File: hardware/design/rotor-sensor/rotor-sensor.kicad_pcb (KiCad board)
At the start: 2 copper layers, 42 x 34.7 mm, 92 parts, among them J2 Conn_01x06, J4 Conn_ARM_JTAG_SWD_10, U1 MCP2021A-xxxE/SN, U2 AP22804AW5, U3 BMI088, U4 AP2127K-ADJTRG1, U5 AP22804AW5, U6 ATSAMD21E18A-A, Y1 ABS07-32.768KHZ-7-T

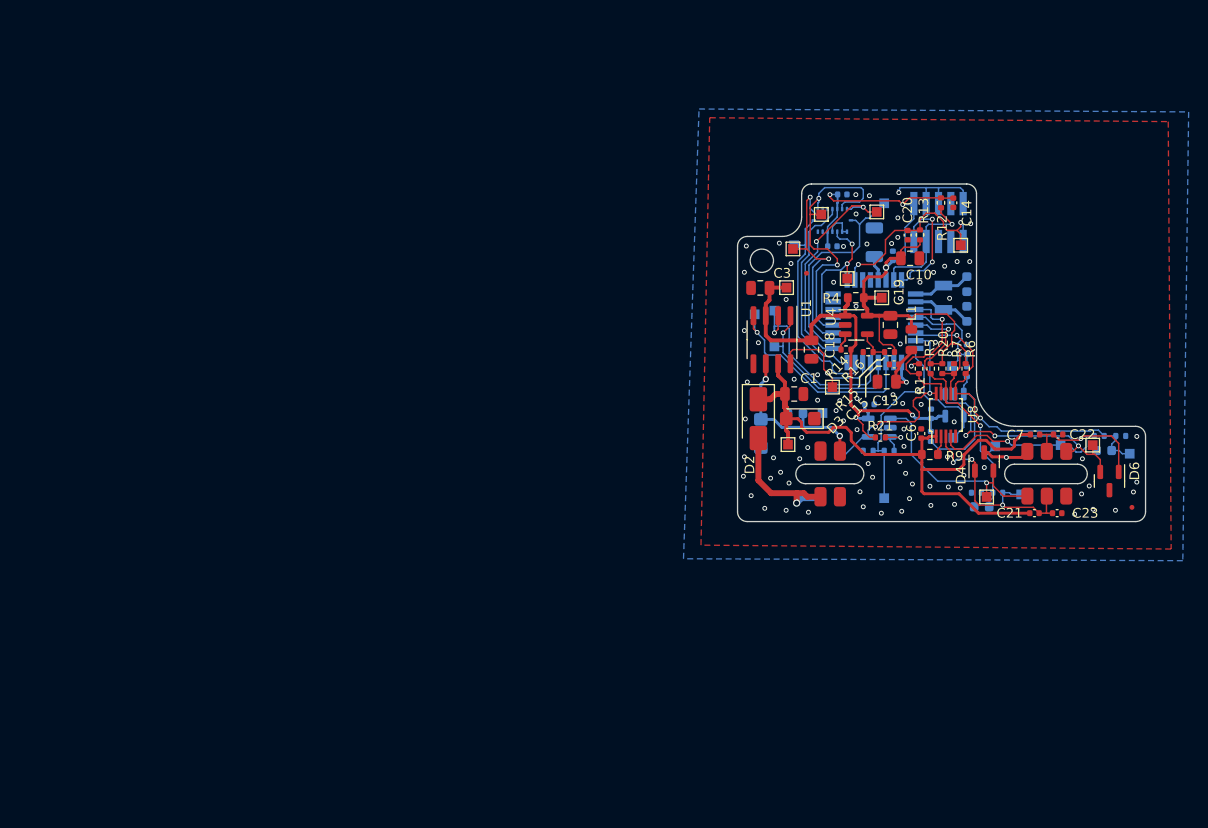
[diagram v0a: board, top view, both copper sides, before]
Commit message: New schematic done
Works with TLIN1028-Q1 transceiver
Added BMP581 pressure sensor
Removed 3wire output stage
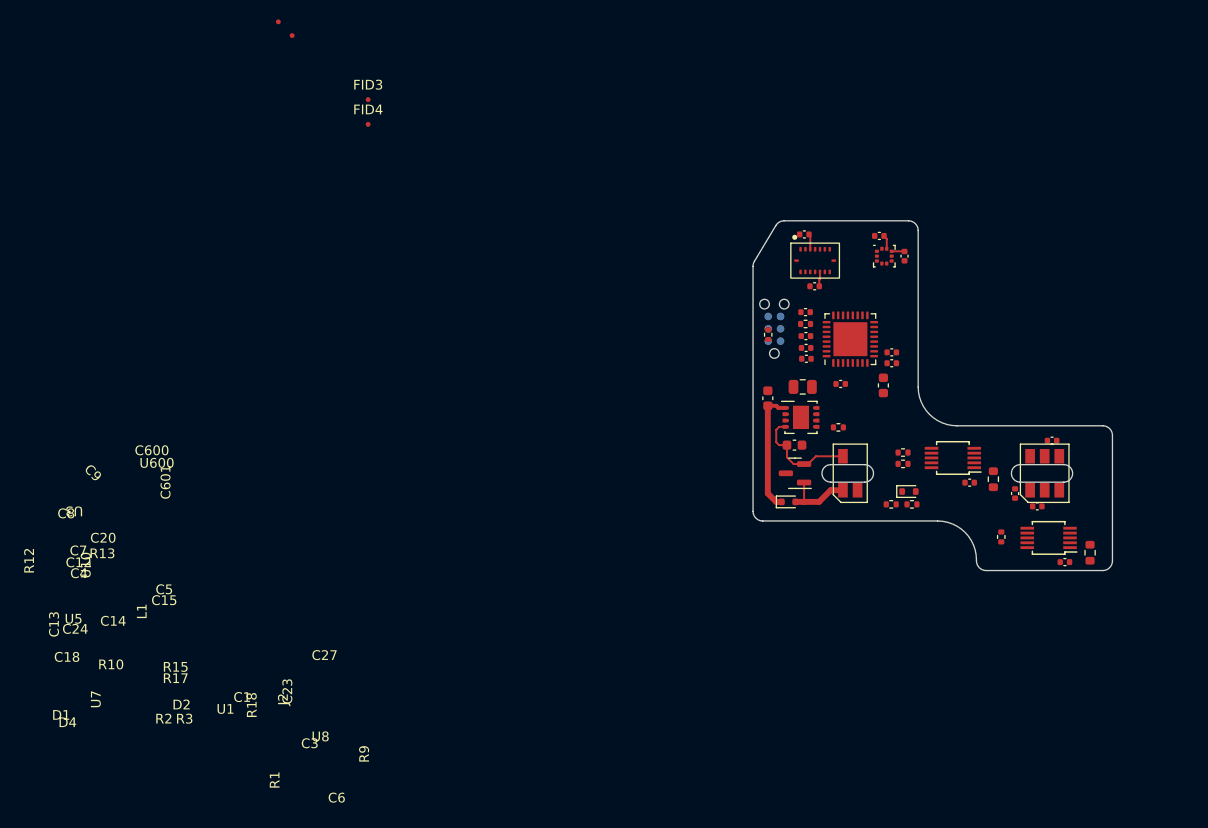
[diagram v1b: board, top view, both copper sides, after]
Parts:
- removed C10, C19: 10u, Capacitor_SMD:C_0805_2012Metric
- removed C11, C16: 6.8p, Capacitor_SMD:C_0603_1608Metric
- removed C17: 1u, Capacitor_SMD:C_1206_3216Metric
- removed C2: 220p, Capacitor_SMD:C_0603_1608Metric
- removed C21, C22: 220n, Capacitor_SMD:C_0402_1005Metric
- removed C25: 22n, Capacitor_SMD:C_0603_1608Metric
- removed D3: SMF33CA-DIO, Diode_SMD:D_SMF
- removed D6: PESD5V0S2BT, Package_TO_SOT_SMD:SOT-23
- removed J4: Conn_ARM_JTAG_SWD_10, Connector_PinHeader_1.27mm:PinHeader_2x05_P1.27mm_Vertical_SMD
- removed R11, R19, R8: 1k, Resistor_SMD:R_0402_1005Metric
- removed R14, R20, R21, R22, R5, R6: 10k, Resistor_SMD:R_0402_1005Metric
- removed R16: 1.5k, Resistor_SMD:R_0402_1005Metric
- removed R4: 0, Resistor_SMD:R_0603_1608Metric
- removed R7: 4.7k, Resistor_SMD:R_0402_1005Metric
- removed TP1: O5, TestPoint:TestPoint_Pad_1.0x1.0mm
- removed TP10: V2, TestPoint:TestPoint_Pad_1.0x1.0mm
- removed TP11: V1, TestPoint:TestPoint_Pad_1.0x1.0mm
- removed TP12: B1, TestPoint:TestPoint_Pad_1.0x1.0mm
- removed TP13: B2, TestPoint:TestPoint_Pad_1.0x1.0mm
- removed TP14: B3, TestPoint:TestPoint_Pad_1.0x1.0mm
- removed TP15: B4, TestPoint:TestPoint_Pad_1.0x1.0mm
- removed TP16: B5, TestPoint:TestPoint_Pad_1.0x1.0mm
- removed TP17: S1, TestPoint:TestPoint_Pad_1.0x1.0mm
- removed TP19: S3, TestPoint:TestPoint_Pad_1.0x1.0mm
- removed TP2: O6, TestPoint:TestPoint_Pad_1.0x1.0mm
- removed TP20: S4, TestPoint:TestPoint_Pad_1.0x1.0mm
- removed TP21: S5, TestPoint:TestPoint_Pad_1.0x1.0mm
- removed TP22: S6, TestPoint:TestPoint_Pad_1.0x1.0mm
- removed TP23: S7, TestPoint:TestPoint_Pad_1.0x1.0mm
- removed TP27: M1, TestPoint:TestPoint_Pad_1.0x1.0mm
- removed TP28: O4, TestPoint:TestPoint_Pad_1.0x1.0mm
- removed TP29: O2, TestPoint:TestPoint_Pad_1.0x1.0mm
- removed TP3: O7, TestPoint:TestPoint_Pad_1.0x1.0mm
- removed TP30: O1, TestPoint:TestPoint_Pad_1.0x1.0mm
- removed TP4: O8, TestPoint:TestPoint_Pad_1.0x1.0mm
- removed TP5: O9, TestPoint:TestPoint_Pad_1.0x1.0mm
- removed TP6: O10, TestPoint:TestPoint_Pad_1.0x1.0mm
- removed TP7: O3, TestPoint:TestPoint_Pad_1.0x1.0mm
- removed TP8: P1, TestPoint:TestPoint_Pad_1.0x1.0mm
- removed TP9: P2, TestPoint:TestPoint_Pad_1.0x1.0mm
- removed U2: AP22804AW5, Package_TO_SOT_SMD:SOT-23-5
- removed U4: AP2127K-ADJTRG1, Package_TO_SOT_SMD:SOT-23-5
- removed U6: ATSAMD21E18A-A, Package_QFP:TQFP-32_7x7mm_P0.8mm
- removed Y1: ABS07-32.768KHZ-7-T, Crystal:Crystal_SMD_3215-2Pin_3.2x1.5mm
- added C27: 100n, Capacitor_SMD:C_0402_1005Metric, F.Cu at (115.6, 75.5)
- added C600: 100n, Capacitor_SMD:C_0402_1005Metric, F.Cu at (97.9, 54.5)
- added C601: 100n, Capacitor_SMD:C_0402_1005Metric, F.Cu at (100.5, 56.5)
- added FID3: Fiducial, Fiducial:Fiducial_0.5mm_Mask1mm, F.Cu at (45.2, 40.4)
- added FID4: Fiducial, Fiducial:Fiducial_0.5mm_Mask1mm, F.Cu at (45.2, 43.0)
- added J1: Conn_ARM_SWD_TagConnect_TC2030-NL, Connector:Tag-Connect_TC2030-IDC-NL_2x03_P1.27mm_Vertical, B.Cu at (87.1, 64.0)
- added U10: ATSAMD21E18A-MUT, Package_DFN_QFN:VQFN-32-1EP_5x5mm_P0.5mm_EP3.5x3.5mm, F.Cu at (94.9, 65.1)
- added U600: ~, local_footprints:Bosch_LGA10, F.Cu at (98.4, 56.5)
- C1, C3: value 10u -> 100n; footprint Capacitor_SMD:C_0805_2012Metric -> Capacitor_SMD:C_0402_1005Metric
- C12, C8, C9: value 220n -> 100n; moved to F.Cu
- C13: value 10u -> 100n; footprint Capacitor_SMD:C_0805_2012Metric -> Capacitor_SMD:C_0603_1608Metric
- C14, C15, C23, C6: value 220n -> 100n
- C18: value 10u -> 220p; footprint Capacitor_SMD:C_0805_2012Metric -> Capacitor_SMD:C_0603_1608Metric
- C24: value 220n -> 22u; footprint Capacitor_SMD:C_0402_1005Metric -> Capacitor_SMD:C_0805_2012Metric; moved to F.Cu
- C4: value 22n -> 10u; footprint Capacitor_SMD:C_0603_1608Metric -> Capacitor_SMD:C_0402_1005Metric; moved to F.Cu
- C5: value 220n -> 10u; moved to F.Cu
- C7: value 220n -> 2.2u
- D1: value SMF33CA-DIO -> BAS3005B02; footprint Diode_SMD:D_SMF -> Diode_SMD:D_SOD-523; moved to F.Cu
- D2: value B140-13-F -> D_Zener; footprint Diode_SMD:D_SMA -> Diode_SMD:D_SOD-523
- D4: value PESD5V0S2BT -> SDT23C15L02
- J2: footprint local_footprints:SMD_6PIN -> local_footprints:SOIC-6
- L1: footprint Inductor_SMD:L_0805_2012Metric -> Inductor_SMD:L_0603_1608Metric
- R10: value 1k -> 10k; moved to F.Cu
- R17: value 1k -> 4.7k; moved to F.Cu
- R18: value 1k -> 63.4k; footprint Resistor_SMD:R_0402_1005Metric -> Resistor_SMD:R_0603_1608Metric; moved to F.Cu
- R2: value 1k -> 47k; moved to F.Cu
- R3: value 1k -> 1.5k; moved to F.Cu
- U1: value MCP2021A-xxxE/SN -> ~; footprint Package_SO:SOIC-8_3.9x4.9mm_P1.27mm -> Package_SO:MSOP-10_3x3mm_P0.5mm
- U3: moved to F.Cu
- U5: value AP22804AW5 -> ~; footprint Package_TO_SOT_SMD:SOT-23-5 -> Package_SON:Texas_S-PVSON-N8; moved to F.Cu
- U7: footprint local_footprints:SMD_4PIN -> local_footprints:SOIC-4
- moved FID1 99.2 mm to (37.4, 33.8)
- moved FID2 60.2 mm to (36.0, 32.4)
- moved C3 36.3 mm to (114.1, 82.3)
- moved C4 32.1 mm to (90.4, 67.1)
- moved C7 25.7 mm to (90.3, 64.8), turned to 0 degrees
- moved R3 22.6 mm to (101.2, 82.1), turned to 0 degrees
- moved R2 22.5 mm to (99.1, 82.1), turned to 0 degrees
- moved R12 22.4 mm to (86.4, 64.6), turned to 90 degrees
- moved U1 22.3 mm to (105.4, 77.3), turned to 180 degrees
- moved C14 22.0 mm to (93.9, 69.7), turned to 180 degrees
- moved C1 20.2 mm to (107.2, 79.9), turned to 0 degrees
- moved C6 19.9 mm to (117.0, 88.0), turned to 0 degrees
- moved D4 19.5 mm to (89.2, 78.9), turned to 180 degrees
- moved R9 19.3 mm to (119.6, 87.1), turned to 90 degrees
- moved R1 19.3 mm to (110.4, 85.4)
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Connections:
- net /M06_SDO renamed /M06_BMI088_MISO
- C13 pad 2: /VDDANA -> +BATT
- C14 pad 2: +3.3V -> /M03_EN
- C18 pad 1: GND -> /M03_LINE
- C18 pad 2: VCC -> GND
- C23 pad 2: /M07_IN1_IN -> /M04_IN3_IN
- C24 pad 1: GND -> +3.3V
- C24 pad 2: VCC -> GND
- C3 pad 1: VCC -> GND
- C3 pad 2: GND -> /M04_IN1_IN
- C4 pad 2: /M04_INPUT2/INPUT2/INPUT2 -> +3.3V
- C5 pad 2: VCC -> /VDDANA
- C7 pad 1: /M07_IN2_IN -> GND
- C7 pad 2: +BATT -> /VDDCORE
- D1 pad 1: GND -> +BATT
- D1 pad 2: Net-(D1-A2) -> VS
- D2 pad 1: +BATT -> /M03_VMON
- D2 pad 2: Net-(D2-A) -> GND
- D4 pad 1: /M07_IN1_IN -> VS
- D4 pad 2: /M07_IN1_VSUP -> /M03_LINE
- J2 pad 1: GND -> /M04_IN1_IN
- J2 pad 2: /M07_IN2_IN -> GND
- J2 pad 3: /M07_IN2_VSUP -> /M04_IN3_IN
- J2 pad 4: /M07_IN1_VSUP -> /M04_IN2_IN
- J2 pad 5: /M07_IN1_IN -> GND
- R1 pad 2: /M04_INPUT1_DIAG/OE/~{FLAG} -> /M04_INPUT3_DIAG/OE
- R10 pad 1: GND -> +3.3V
- R10 pad 2: /M04_INPUT2_DIAG/INPUT1/~{FLAG} -> /M03_RXD
- R15 pad 1: Net-(U4-ADJ) -> GND
- R15 pad 2: +3.3V -> /M04_INPUT2_DIAG/INPUT1
- R17 pad 2: /M04_INPUT1_DIAG/OE/~{FLAG} -> /M04_INPUT1_DIAG/OE
- R18 pad 1: GND -> +BATT
- R18 pad 2: /M04_INPUT1/~{ERR}/INPUT1 -> Net-(U1-ISET)
- R2 pad 1: /M04_INPUT2/INPUT2/INPUT2 -> +BATT
- R2 pad 2: /M07_IN2_IN -> /M03_VMON
- R3 pad 1: GND -> /M03_VMON
- R3 pad 2: /M04_INPUT2/INPUT2/INPUT2 -> GND
- U1 pad 1: /M02_RXD -> +BATT
- U1 pad 2: /M02_CS -> Net-(U1-ISET)
- U1 pad 3: VCC -> /M04_IN1_IN
- U1 pad 4: /M02_TXD -> /M04_IN2_IN
- U1 pad 6: Net-(D1-A2) -> /M04_INPUT2/INPUT2
- U1 pad 7: +BATT -> /M04_INPUT2_DIAG/INPUT1
- U1 pad 8: /M02_TXE -> /M04_INPUT1/~{ERR}
- U3 pad 12: /M06_GYRO_INT -> unconnected-(U3-INT3-Pad12)
- U3 pad 14: /M06_CS_ACCEL -> /M06_BMI088_CSA
- U3 pad 16: /M06_ACCEL_INT -> unconnected-(U3-INT1-Pad16)
- U3 pad 5: /M06_CS_GYRO -> /M06_BMI088_CSG
- U3 pad 8: /M06_SCK -> /M05_BMI088_SCK
- U3 pad 9: /M06_SDI -> /M05_BMI088_MOSI
- U5 pad 1: /M07_IN1_VSUP -> +BATT
- U5 pad 2: GND -> /M03_EN
- U5 pad 3: Net-(U5-~{FLG}) -> GND
- U5 pad 4: /M04_~{SLEEP}/DIAG/EN1 -> /M03_LINE
- U5 pad 5: VCC -> /M03_RXD
- U7 pad 1: Net-(D2-A) -> VS
- U7 pad 2: unconnected-(U7-Pad2) -> GND
- U7 pad 3: Net-(D1-A2) -> /M03_LINE
- U8 pad 10: /M04_~{SLEEP}/DIAG/EN1 -> /M04_~{SLEEP2}/DIAG2
- U8 pad 3: /M07_IN1_IN -> /M04_IN3_IN
- U8 pad 4: /M07_IN2_IN -> +BATT
- U8 pad 6: /M04_INPUT2/INPUT2/INPUT2 -> unconnected-(U8-DOUT2-Pad6)
- U8 pad 7: /M04_INPUT2_DIAG/INPUT1/~{FLAG} -> /M04_NC/INPUT3
- U8 pad 8: /M04_INPUT1/~{ERR}/INPUT1 -> /M04_INPUT3/~{ERR}
- U8 pad 9: /M04_INPUT1_DIAG/OE/~{FLAG} -> /M04_INPUT3_DIAG/OE
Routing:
- net +3.3V: track 70.1 -> 5.86 mm, vias 3 -> 0
- net +BATT: track 61.8 -> 12.8 mm
- net VCC: track 48.2 -> 0.00 mm, vias 2 -> 0
- net /M04_INPUT2/INPUT2/INPUT2: track 34.9 -> 0.00 mm, vias 2 -> 0
- net /M07_IN2_IN: track 32.7 -> 0.00 mm, vias 2 -> 0
- net /M04_INPUT1_DIAG/OE/~{FLAG}: track 32.4 -> 0.00 mm, vias 2 -> 0
- net /M06_BMI088_MISO: track 30.0 -> 0.00 mm, vias 2 -> 0
- net /M04_INPUT1/~{ERR}/INPUT1: track 29.9 -> 0.00 mm, vias 2 -> 0
- net /M07_IN2_VSUP: track 25.5 -> 0.00 mm, vias 3 -> 0
- net /M02_TXD: track 23.3 -> 0.00 mm, vias 1 -> 0
- net /M06_CS_ACCEL: track 23.2 -> 0.00 mm, vias 2 -> 0
- net /M06_SDI: track 23.1 -> 0.00 mm, vias 2 -> 0
- net /M07_IN1_IN: track 23.0 -> 0.00 mm, vias 3 -> 0
- net /M06_ACCEL_INT: track 22.6 -> 0.00 mm
- net /M07_IN1_VSUP: track 22.2 -> 0.00 mm, vias 1 -> 0
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- removed copper zone on B.Cu, net GND
- removed copper zone on F.Cu, net GND
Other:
- board size 42 x 34.7 mm -> 37 x 36 mm

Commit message: FInal ordered hardware
New 3pin connector
Extra 2pin connector for cadence measurement
No 3pin sensor variant
DC/DC converter for MCU
Pressure sensor
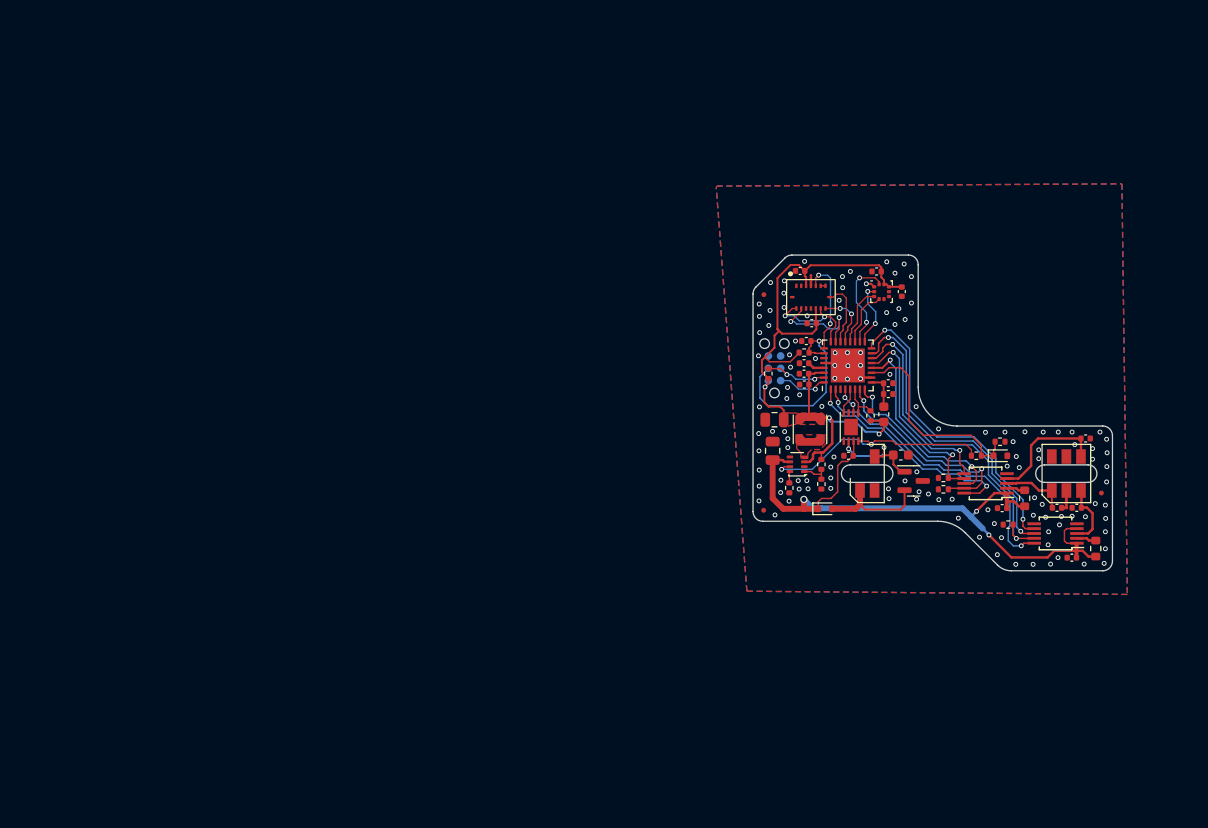
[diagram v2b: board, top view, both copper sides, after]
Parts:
- removed C13: 100n, Capacitor_SMD:C_0603_1608Metric
- removed C14: 100n, Capacitor_SMD:C_0402_1005Metric
- removed C18: 220p, Capacitor_SMD:C_0603_1608Metric
- removed C24: 22u, Capacitor_SMD:C_0805_2012Metric
- removed FID2: Fiducial, Fiducial:Fiducial_0.5mm_Mask1mm
- removed R10: 10k, Resistor_SMD:R_0402_1005Metric
- removed U5: ~, Package_SON:Texas_S-PVSON-N8
- added C10: 220p, Capacitor_SMD:C_0603_1608Metric, F.Cu at (100.1, 77.0)
- added C11: 22u, Capacitor_SMD:C_0805_2012Metric, F.Cu at (87.1, 73.4)
- added C16: 10u, Capacitor_SMD:C_0805_2012Metric, F.Cu at (86.9, 76.6)
- added C2: 100n, Capacitor_SMD:C_0402_1005Metric, F.Cu at (94.7, 77.1)
- added L3: 2.2u, Inductor_SMD:L_Coilcraft_LPS3010, F.Cu at (90.7, 74.4)
- added R4: 4.7k, Resistor_SMD:R_0402_1005Metric, F.Cu at (97.0, 73.0)
- added R5: 20k, Resistor_SMD:R_0402_1005Metric, F.Cu at (91.9, 78.0)
- added R6: 4.7k, Resistor_SMD:R_0402_1005Metric, F.Cu at (91.9, 80.0)
- added R7: 0, Resistor_SMD:R_0402_1005Metric, F.Cu at (88.6, 80.4)
- added U2: MCP2003BT-E/MC, Package_DFN_QFN:DFN-8-1EP_3x2mm_P0.5mm_EP1.7x1.4mm, F.Cu at (95.0, 74.1)
- added U6: TPS629210DRLR, Package_TO_SOT_SMD:SOT-583-8, F.Cu at (89.4, 78.0)
- C20: value 220n -> 100n
- D2: value D_Zener -> MM5Z3V6T1G
- R3: value 1.5k -> 4.7k
- U1, U8: value ~ -> MAX9621AUB+T
- U600: value ~ -> BMP581
- moved FID4 84.5 mm to (120.7, 80.9)
- moved FID1 68.9 mm to (86.0, 82.7)
- moved FID3 45.4 mm to (86.0, 60.5)
- moved D4 12.2 mm to (101.4, 79.7), turned to 0 degrees
- moved R3 11.1 mm to (110.3, 75.6)
- moved D2 10.1 mm to (110.3, 77.1)
- moved R2 10.1 mm to (107.8, 77.1)
- moved C23 6.52 mm to (118.2, 82.4), turned to 0 degrees
- moved R15 4.91 mm to (104.5, 79.4)
- moved R17 4.91 mm to (104.5, 80.5)
- moved U1 4.26 mm to (108.8, 79.9)
- moved C1 4.25 mm to (110.5, 82.5)
- moved J1 4.07 mm to (87.1, 68.1)
- moved R12 4.00 mm to (86.4, 68.6)
- moved D1 3.83 mm to (92.3, 82.5)
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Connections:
- D4 pad 1: VS -> /M03_LINE
- D4 pad 2: /M03_LINE -> VS
- R2 pad 1: +BATT -> /M03_REGEN
- U10 pad 11: /M04_INPUT2_DIAG/INPUT1 -> /M03_VMON
- U10 pad 12: /M04_INPUT2/INPUT2 -> /M04_INPUT2_DIAG/INPUT1
- U10 pad 13: /M04_INPUT3_DIAG/OE -> /M04_INPUT2/INPUT2
- U10 pad 14: /M04_INPUT3/~{ERR} -> /M04_INPUT3_DIAG/OE
- U10 pad 15: /M04_NC/INPUT3 -> /M04_INPUT3/~{ERR}
- U10 pad 16: unconnected-(U10-PA15-Pad16) -> /M04_NC/INPUT3
- U10 pad 3: /M03_VMON -> unconnected-(U10-PA02-Pad3)
- U10 pad 33: (no net) -> GND
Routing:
- net +3.3V: track 5.86 -> 70.3 mm, vias 0 -> 3
- net +BATT: track 12.8 -> 67.9 mm, vias 0 -> 3
- net /M04_INPUT3_DIAG/OE: track 0.00 -> 34.0 mm, vias 0 -> 2
- net /M04_INPUT3/~{ERR}: track 0.00 -> 32.5 mm, vias 0 -> 2
- net /M04_NC/INPUT3: track 0.00 -> 32.4 mm, vias 0 -> 2
- net /M04_~{SLEEP2}/DIAG2: track 0.00 -> 30.7 mm, vias 0 -> 2
- net /M03_REGEN: track 0.00 -> 24.6 mm, vias 0 -> 2
- net /M04_~{SLEEP1}/DIAG1: track 0.00 -> 23.8 mm, vias 0 -> 2
- net /M04_INPUT1_DIAG/OE: track 0.00 -> 22.4 mm, vias 0 -> 2
- net /M03_VMON: track 0.00 -> 21.4 mm
- net /M05_RESET: track 0.00 -> 20.4 mm, vias 0 -> 1
- net /M04_INPUT2_DIAG/INPUT1: track 0.00 -> 20.1 mm, vias 0 -> 2
- net /M04_INPUT2/INPUT2: track 0.00 -> 19.8 mm, vias 0 -> 2
- net /M04_INPUT1/~{ERR}: track 0.00 -> 18.5 mm, vias 0 -> 2
- net /M04_IN2_IN: track 0.00 -> 12.4 mm
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- added copper zone on F.Cu, net +3.3V
- added copper zone on F.Cu, net /TPS629210_SW
- added copper zone on B.Cu, net GND
- added copper zone on F.Cu, net GND
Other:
- board size 37 x 36 mm -> 37 x 32.5 mm
